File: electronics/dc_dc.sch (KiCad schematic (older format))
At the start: 18 parts

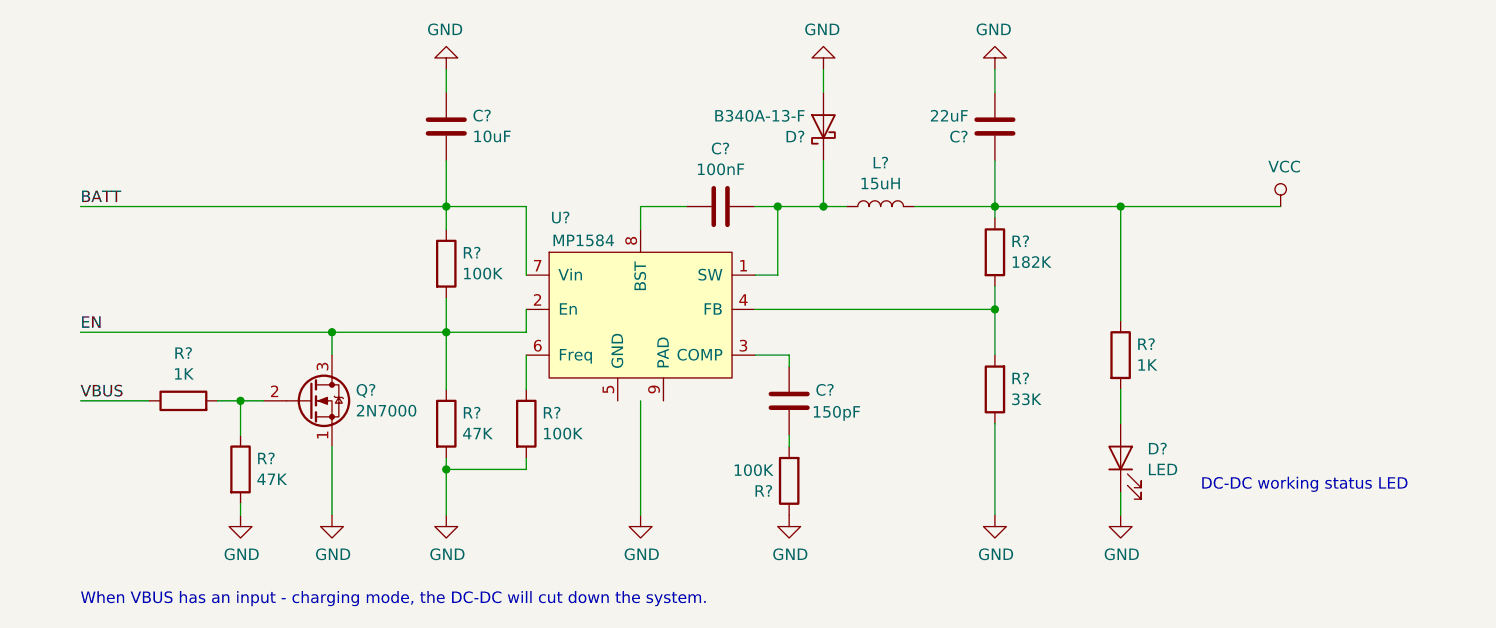
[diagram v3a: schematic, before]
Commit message: Preview SCH is done, but not fully finished.
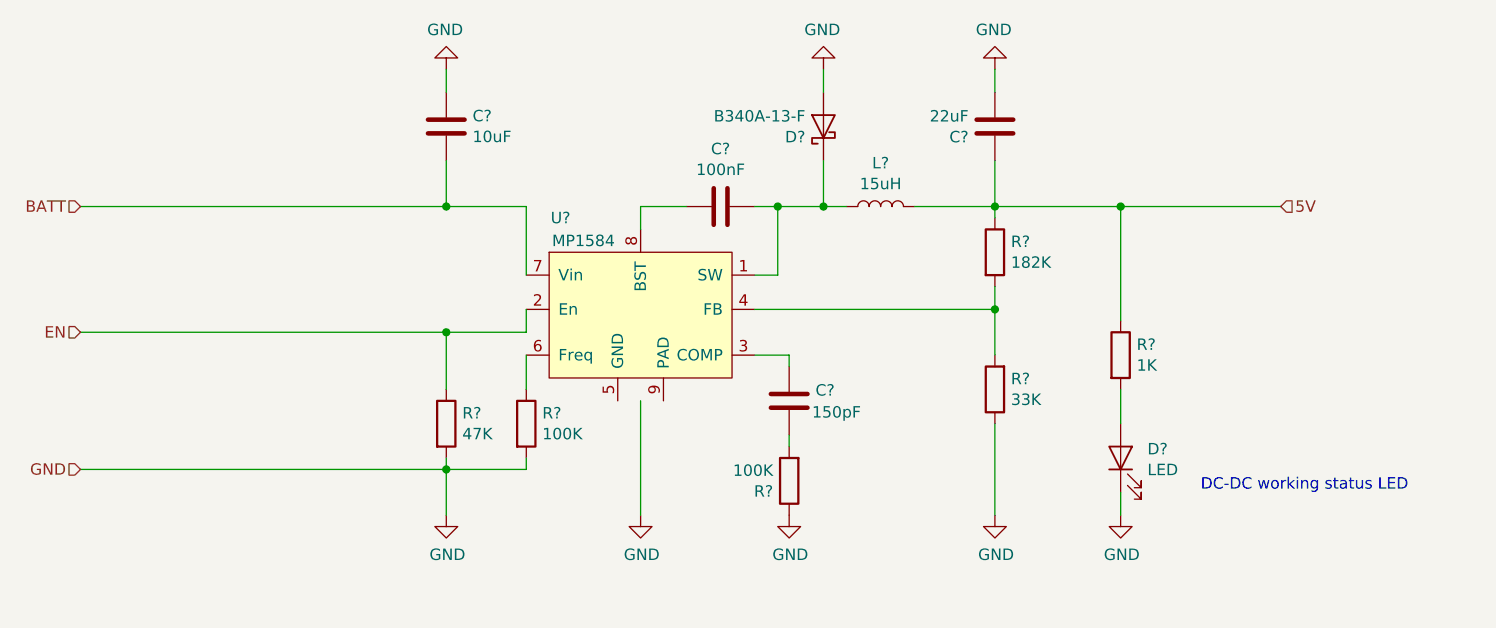
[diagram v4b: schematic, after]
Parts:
- removed Q?: 2N7000, Package_TO_SOT_SMD:SOT-23, symbol Transistor_FET:2N7000
- removed R?: 100K, Resistor_SMD:R_0805_2012Metric, symbol Device:R
- removed R?: 1K, Resistor_SMD:R_0805_2012Metric, symbol Device:R
- removed R?: 47K, Resistor_SMD:R_0805_2012Metric, symbol Device:R
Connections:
- net VCC renamed 5V
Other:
- note removed: "When VBUS has an input - charging mode, the DC-DC will cut down the system."
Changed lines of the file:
@@
 $Descr A4 11693 8268
 encoding utf-8
-Sheet 2 4
+Sheet 3 4
 Title ""
 Date ""
@@
 $Comp
 L Device:R R?
-U 1 1 5E8D0879
-P 4850 3600
-F 0 "R?" H 4920 3646 50  0000 L CNN
-F 1 "100K" H 4920 3555 50  0000 L CNN
-F 2 "Resistor_SMD:R_0805_2012Metric" V 4780 3600 50  0001 C CNN
-F 3 "~" H 4850 3600 50  0001 C CNN
-	1    4850 3600
-	1    0    0    -1
-$EndComp
-$Comp
-L Device:R R?
 U 1 1 5E8D0E3C
 P 4850 4300
@@
 $EndComp
 $Comp
-L power:GND #PWR?
+L power:GND #PWR0119
 U 1 1 5E8D8C44
 P 4850 4700
-F 0 "#PWR?" H 4850 4450 50  0001 C CNN
+F 0 "#PWR0119" H 4850 4450 50  0001 C CNN
 F 1 "GND" H 4855 4527 50  0000 C CNN
 F 2 "" H 4850 4700 50  0001 C CNN
@@
 	6300 3350 6200 3350
 $Comp
-L power:GND #PWR?
+L power:GND #PWR0120
 U 1 1 5E8E265E
 P 5700 4700
-F 0 "#PWR?" H 5700 4450 50  0001 C CNN
+F 0 "#PWR0120" H 5700 4450 50  0001 C CNN
 F 1 "GND" H 5705 4527 50  0000 C CNN
 F 2 "" H 5700 4700 50  0001 C CNN
@@
 	6350 4350 6350 4400
 $Comp
-L power:GND #PWR?
+L power:GND #PWR0121
 U 1 1 5E8E80EC
 P 6350 4700
-F 0 "#PWR?" H 6350 4450 50  0001 C CNN
+F 0 "#PWR0121" H 6350 4450 50  0001 C CNN
 F 1 "GND" H 6355 4527 50  0000 C CNN
 F 2 "" H 6350 4700 50  0001 C CNN
@@
 $EndComp
 $Comp
-L power:GND #PWR?
+L power:GND #PWR0122
 U 1 1 5E8F0C8B
 P 6500 2750
-F 0 "#PWR?" H 6500 2500 50  0001 C CNN
+F 0 "#PWR0122" H 6500 2500 50  0001 C CNN
 F 1 "GND" H 6505 2577 50  0000 C CNN
 F 2 "" H 6500 2750 50  0001 C CNN
@@
 $EndComp
 $Comp
-L power:GND #PWR?
+L power:GND #PWR0123
 U 1 1 5E8F68C8
 P 7250 2750
-F 0 "#PWR?" H 7250 2500 50  0001 C CNN
+F 0 "#PWR0123" H 7250 2500 50  0001 C CNN
 F 1 "GND" H 7255 2577 50  0000 C CNN
 F 2 "" H 7250 2750 50  0001 C CNN
@@
 	7250 4300 7250 4700
 $Comp
-L power:GND #PWR?
+L power:GND #PWR0124
 U 1 1 5E8FFCF0
 P 7250 4700
-F 0 "#PWR?" H 7250 4450 50  0001 C CNN
+F 0 "#PWR0124" H 7250 4450 50  0001 C CNN
 F 1 "GND" H 7255 4527 50  0000 C CNN
 F 2 "" H 7250 4700 50  0001 C CNN
@@
 	1    0    0    -1
 $EndComp
-Wire Wire Line
-	4850 3350 4850 3450
 Connection ~ 4850 3350
-Wire Wire Line
-	4850 3750 4850 3900
-Text Label 3250 3350 0    50   ~ 0
-BATT
-Text Label 3250 3900 0    50   ~ 0
-EN
 Wire Wire Line
 	5200 3350 5200 3650
@@
 	4850 2850 4850 2750
 $Comp
-L power:GND #PWR?
+L power:GND #PWR0125
 U 1 1 5E932930
 P 4850 2750
-F 0 "#PWR?" H 4850 2500 50  0001 C CNN
+F 0 "#PWR0125" H 4850 2500 50  0001 C CNN
 F 1 "GND" H 4855 2577 50  0000 C CNN
 F 2 "" H 4850 2750 50  0001 C CNN
@@
 Wire Wire Line
 	7250 3150 7250 3350
-$Comp
-L power:VCC #PWR?
-U 1 1 5E935E86
-P 8500 3350
-F 0 "#PWR?" H 8500 3200 50  0001 C CNN
-F 1 "VCC" H 8517 3523 50  0000 C CNN
-F 2 "" H 8500 3350 50  0001 C CNN
-F 3 "" H 8500 3350 50  0001 C CNN
-	1    8500 3350
-	1    0    0    -1
-$EndComp
 $Comp
 L Device:R R?
@@
 	7800 4600 7800 4700
 $Comp
-L power:GND #PWR?
+L power:GND #PWR0126
 U 1 1 5E93DD7B
 P 7800 4700
-F 0 "#PWR?" H 7800 4450 50  0001 C CNN
+F 0 "#PWR0126" H 7800 4450 50  0001 C CNN
 F 1 "GND" H 7805 4527 50  0000 C CNN
 F 2 "" H 7800 4700 50  0001 C CNN
@@
 Wire Wire Line
 	7800 3350 8500 3350
-$Comp
-L Transistor_FET:2N7000 Q?
-U 1 1 5E941285
-P 4250 4200
-F 0 "Q?" H 4454 4246 50  0000 L CNN
-F 1 "2N7000" H 4454 4155 50  0000 L CNN
-F 2 "Package_TO_SOT_SMD:SOT-23" H 4450 4125 50  0001 L CIN
-F 3 "https://www.fairchildsemi.com/datasheets/2N/2N7000.pdf" H 4250 4200 50  0001 L CNN
-	1    4250 4200
-	1    0    0    -1
-$EndComp
-$Comp
-L power:GND #PWR?
-U 1 1 5E94311E
-P 4350 4700
-F 0 "#PWR?" H 4350 4450 50  0001 C CNN
-F 1 "GND" H 4355 4527 50  0000 C CNN
-F 2 "" H 4350 4700 50  0001 C CNN
-F 3 "" H 4350 4700 50  0001 C CNN
-	1    4350 4700
-	1    0    0    -1
-$EndComp
-Wire Wire Line
-	4350 4400 4350 4700
-Wire Wire Line
-	4350 3900 4350 4000
-$Comp
-L Device:R R?
-U 1 1 5E9453A6
-P 3700 4200
-F 0 "R?" V 3907 4200 50  0000 C CNN
-F 1 "1K" V 3816 4200 50  0000 C CNN
-F 2 "Resistor_SMD:R_0805_2012Metric" V 3630 4200 50  0001 C CNN
-F 3 "~" H 3700 4200 50  0001 C CNN
-	1    3700 4200
-	0    -1   -1   0
-$EndComp
-$Comp
-L Device:R R?
-U 1 1 5E94608A
-P 3950 4500
-F 0 "R?" H 4020 4546 50  0000 L CNN
-F 1 "47K" H 4020 4455 50  0000 L CNN
-F 2 "Resistor_SMD:R_0805_2012Metric" V 3880 4500 50  0001 C CNN
-F 3 "~" H 3950 4500 50  0001 C CNN
-	1    3950 4500
-	1    0    0    -1
-$EndComp
-Connection ~ 4350 3900
-Wire Wire Line
-	4350 3900 4850 3900
-Wire Wire Line
-	3250 3900 4350 3900
-$Comp
-L power:GND #PWR?
-U 1 1 5E94BF0D
-P 3950 4700
-F 0 "#PWR?" H 3950 4450 50  0001 C CNN
-F 1 "GND" H 3955 4527 50  0000 C CNN
-F 2 "" H 3950 4700 50  0001 C CNN
-F 3 "" H 3950 4700 50  0001 C CNN
-	1    3950 4700
-	1    0    0    -1
-$EndComp
-Wire Wire Line
-	3850 4200 3950 4200
-Wire Wire Line
-	3950 4350 3950 4200
-Connection ~ 3950 4200
-Wire Wire Line
-	3950 4200 4050 4200
-Wire Wire Line
-	3950 4650 3950 4700
-Wire Wire Line
-	3550 4200 3250 4200
-Text Label 3250 4200 0    50   ~ 0
-VBUS
-Text Notes 3250 5100 0    50   ~ 0
-When VBUS has an input - charging mode, the DC-DC will cut down the system.
 Text Notes 8150 4600 0    50   ~ 0
 DC-DC working status LED
+Text HLabel 3250 3350 0    50   Input ~ 0
+BATT
+Text HLabel 3250 3900 0    50   Input ~ 0
+EN
+Wire Wire Line
+	3250 3900 4850 3900
+Text HLabel 8500 3350 2    50   Input ~ 0
+5V
+Text HLabel 3250 4500 0    50   Input ~ 0
+GND
+Wire Wire Line
+	3250 4500 4850 4500
 $EndSCHEMATC

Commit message: modified:   ../../electronics/charger.sch 	modified:   ../../electronics/charger.sch-bak 	modified:   ../../electronics/dc_dc.sch 	modified:   ../../electronics/dc_dc.sch-bak 	modified:   ../../electronics/langpie.pro 	modified:   ../../electronics/langpie.sch 	modified:   ../../electronics/langpie.sch-bak 	modified:   ../../electronics/motor_driver_rpi_pi.sch 	modified:   ../../electronics/motor_driver_rpi_pi.sch-bak 	modified:   ../../electronics/schematic_v1_preview.pdf
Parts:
- gave numbers to parts that had none: 14
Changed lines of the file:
@@
 $EndDescr
 $Comp
-L langpie:MP1584 U?
+L langpie:MP1584 U2
 U 1 1 5E8CC2D7
 P 5300 3550
-F 0 "U?" H 5350 3700 50  0000 C CNN
+F 0 "U2" H 5350 3700 50  0000 C CNN
 F 1 "MP1584" H 5450 3600 50  0000 C CNN
 F 2 "Package_SO:SOIC-8-1EP_3.9x4.9mm_P1.27mm_EP2.29x3mm_ThermalVias" H 5450 3650 50  0001 C CNN
@@
 $EndComp
 $Comp
-L Device:C C?
+L Device:C C8
 U 1 1 5E8CFB92
 P 4850 3000
-F 0 "C?" H 4965 3046 50  0000 L CNN
+F 0 "C8" H 4965 3046 50  0000 L CNN
 F 1 "10uF" H 4965 2955 50  0000 L CNN
 F 2 "Capacitor_SMD:C_1206_3216Metric" H 4888 2850 50  0001 C CNN
@@
 $EndComp
 $Comp
-L Device:C C?
+L Device:C C9
 U 1 1 5E8D01BD
 P 6050 3350
-F 0 "C?" V 5798 3350 50  0000 C CNN
+F 0 "C9" V 5798 3350 50  0000 C CNN
 F 1 "100nF" V 5889 3350 50  0000 C CNN
 F 2 "Capacitor_SMD:C_0805_2012Metric" H 6088 3200 50  0001 C CNN
@@
 $EndComp
 $Comp
-L Device:R R?
+L Device:R R13
 U 1 1 5E8D0E3C
 P 4850 4300
-F 0 "R?" H 4920 4346 50  0000 L CNN
+F 0 "R13" H 4920 4346 50  0000 L CNN
 F 1 "47K" H 4920 4255 50  0000 L CNN
 F 2 "Resistor_SMD:R_0805_2012Metric" V 4780 4300 50  0001 C CNN
@@
 $EndComp
 $Comp
-L Device:C C?
+L Device:C C11
 U 1 1 5E8D269D
 P 7250 3000
-F 0 "C?" H 7365 3046 50  0000 L CNN
+F 0 "C11" H 7365 3046 50  0000 L CNN
 F 1 "22uF" H 7365 2955 50  0000 L CNN
 F 2 "Capacitor_SMD:C_1206_3216Metric" H 7288 2850 50  0001 C CNN
@@
 $EndComp
 $Comp
-L Device:C C?
+L Device:C C10
 U 1 1 5E8D2B29
 P 6350 4200
-F 0 "C?" H 6465 4246 50  0000 L CNN
+F 0 "C10" H 6465 4246 50  0000 L CNN
 F 1 "150pF" H 6450 4150 50  0000 L CNN
 F 2 "Capacitor_SMD:C_0805_2012Metric" H 6388 4050 50  0001 C CNN
@@
 $EndComp
 $Comp
-L Device:R R?
+L Device:R R16
 U 1 1 5E8D49A8
 P 7250 3550
-F 0 "R?" H 7320 3596 50  0000 L CNN
+F 0 "R16" H 7320 3596 50  0000 L CNN
 F 1 "182K" H 7320 3505 50  0000 L CNN
 F 2 "Resistor_SMD:R_0805_2012Metric" V 7180 3550 50  0001 C CNN
@@
 $EndComp
 $Comp
-L Device:R R?
+L Device:R R15
 U 1 1 5E8D4DEA
 P 6350 4550
-F 0 "R?" H 6420 4596 50  0000 L CNN
+F 0 "R15" H 6420 4596 50  0000 L CNN
 F 1 "100K" H 6420 4505 50  0000 L CNN
 F 2 "Resistor_SMD:R_0805_2012Metric" V 6280 4550 50  0001 C CNN
@@
 $EndComp
 $Comp
-L Device:R R?
+L Device:R R14
 U 1 1 5E8D735B
 P 5200 4300
-F 0 "R?" H 5270 4346 50  0000 L CNN
+F 0 "R14" H 5270 4346 50  0000 L CNN
 F 1 "100K" H 5270 4255 50  0000 L CNN
 F 2 "Resistor_SMD:R_0805_2012Metric" V 5130 4300 50  0001 C CNN
@@
 	5700 4200 5700 4700
 $Comp
-L Device:R R?
+L Device:R R17
 U 1 1 5E8ED7C3
 P 7250 4150
-F 0 "R?" H 7180 4104 50  0000 R CNN
+F 0 "R17" H 7180 4104 50  0000 R CNN
 F 1 "33K" H 7180 4195 50  0000 R CNN
 F 2 "Resistor_SMD:R_0805_2012Metric" V 7180 4150 50  0001 C CNN
@@
 $EndComp
 $Comp
-L Device:L L?
+L Device:L L1
 U 1 1 5E8EE125
 P 6750 3350
-F 0 "L?" V 6940 3350 50  0000 C CNN
+F 0 "L1" V 6940 3350 50  0000 C CNN
 F 1 "15uH" V 6849 3350 50  0000 C CNN
 F 2 "Inductor_SMD:L_12x12mm_H6mm" H 6750 3350 50  0001 C CNN
@@
 $EndComp
 $Comp
-L Device:D_Schottky D?
+L Device:D_Schottky D2
 U 1 1 5E8EE734
 P 6500 3000
-F 0 "D?" V 6454 3079 50  0000 L CNN
+F 0 "D2" V 6454 3079 50  0000 L CNN
 F 1 "B340A-13-F" V 6545 3079 50  0000 L CNN
 F 2 "Diode_SMD:D_SMA" H 6500 3000 50  0001 C CNN
@@
 	7250 3150 7250 3350
 $Comp
-L Device:R R?
+L Device:R R18
 U 1 1 5E938B26
 P 7800 4000
-F 0 "R?" H 7870 4046 50  0000 L CNN
+F 0 "R18" H 7870 4046 50  0000 L CNN
 F 1 "1K" H 7870 3955 50  0000 L CNN
 F 2 "Resistor_SMD:R_0805_2012Metric" V 7730 4000 50  0001 C CNN
@@
 $EndComp
 $Comp
-L Device:LED D?
+L Device:LED D3
 U 1 1 5E939213
 P 7800 4450
-F 0 "D?" V 7839 4333 50  0000 R CNN
+F 0 "D3" V 7839 4333 50  0000 R CNN
 F 1 "LED" V 7748 4333 50  0000 R CNN
 F 2 "LED_SMD:LED_0805_2012Metric" H 7800 4450 50  0001 C CNN

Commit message: Finish PCB, silightly change to SCH, Gerber generated, V1.0 HW almost done.
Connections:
- net GND: now also U2.5 (GND), U2.9 (PAD)
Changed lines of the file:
@@
 $EndDescr
-$Comp
-L langpie:MP1584 U2
-U 1 1 5E8CC2D7
-P 5300 3550
-F 0 "U2" H 5350 3700 50  0000 C CNN
-F 1 "MP1584" H 5450 3600 50  0000 C CNN
-F 2 "Package_SO:SOIC-8-1EP_3.9x4.9mm_P1.27mm_EP2.29x3mm_ThermalVias" H 5450 3650 50  0001 C CNN
-F 3 "https://www.monolithicpower.com/en/documentview/productdocument/index/version/2/document_type/Datasheet/lang/en/sku/MP1584/document_id/204" H 5450 3650 50  0001 C CNN
-	1    5300 3550
-	1    0    0    -1
-$EndComp
 $Comp
 L Device:C C8
@@
 Wire Wire Line
 	6350 4000 6350 4050
-Wire Wire Line
-	5700 4200 5700 4700
 $Comp
 L Device:R R17
@@
 Wire Wire Line
 	3250 4500 4850 4500
+$Comp
+L langpie:MP1584 U2
+U 1 1 5EA1C0D5
+P 5300 3550
+F 0 "U2" H 5350 3800 50  0000 C CNN
+F 1 "MP1584" H 5450 3700 50  0000 C CNN
+F 2 "Package_SO:SOIC-8-1EP_3.9x4.9mm_P1.27mm_EP2.29x3mm_ThermalVias" H 5650 3650 50  0001 C CNN
+F 3 "https://www.monolithicpower.com/en/documentview/productdocument/index/version/2/document_type/Datasheet/lang/en/sku/MP1584/document_id/204" H 5450 3650 50  0001 C CNN
+	1    5300 3550
+	1    0    0    -1
+$EndComp
+Wire Wire Line
+	5600 4350 5700 4350
+Connection ~ 5700 4350
+Wire Wire Line
+	5700 4350 5700 4700
+Wire Wire Line
+	5800 4200 5800 4350
+Wire Wire Line
+	5800 4350 5700 4350
+Wire Wire Line
+	5600 4200 5600 4350
 $EndSCHEMATC
